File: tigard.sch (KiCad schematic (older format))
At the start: 91 parts, among them J1 USB_C_Receptacle_USB2.0, J2 JTAG, J3 UART, J4 SPI, J5 CORTEX, J6 LA, J7 I2C, Q1 BSH103, SW1 TARGET, SW2 MODE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

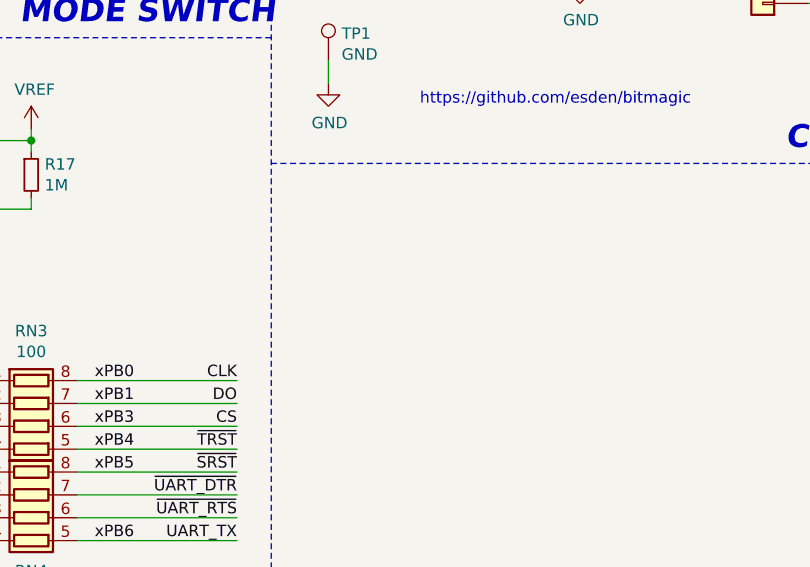
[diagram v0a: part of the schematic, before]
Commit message: Add fidutials
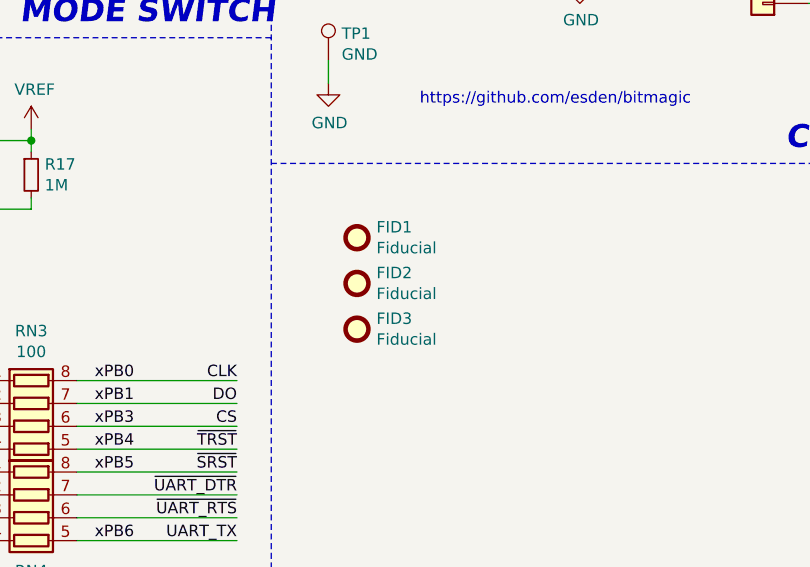
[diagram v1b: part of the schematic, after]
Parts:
- added FID1, FID2, FID3: Fiducial, Fiducial:Fiducial_0.5mm_Mask1mm, symbol Mechanical:Fiducial
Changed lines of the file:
@@
 Wire Wire Line
 	2600 4100 2600 4150
+$Comp
+L Mechanical:Fiducial FID1
+U 1 1 60A39755
+P 9175 4925
+F 0 "FID1" H 9260 4971 50  0000 L CNN
+F 1 "Fiducial" H 9260 4880 50  0000 L CNN
+F 2 "Fiducial:Fiducial_0.5mm_Mask1mm" H 9175 4925 50  0001 C CNN
+F 3 "~" H 9175 4925 50  0001 C CNN
+	1    9175 4925
+	1    0    0    -1
+$EndComp
+$Comp
+L Mechanical:Fiducial FID2
+U 1 1 60A39B2D
+P 9175 5125
+F 0 "FID2" H 9260 5171 50  0000 L CNN
+F 1 "Fiducial" H 9260 5080 50  0000 L CNN
+F 2 "Fiducial:Fiducial_0.5mm_Mask1mm" H 9175 5125 50  0001 C CNN
+F 3 "~" H 9175 5125 50  0001 C CNN
+	1    9175 5125
+	1    0    0    -1
+$EndComp
+$Comp
+L Mechanical:Fiducial FID3
+U 1 1 60A39E45
+P 9175 5325
+F 0 "FID3" H 9260 5371 50  0000 L CNN
+F 1 "Fiducial" H 9260 5280 50  0000 L CNN
+F 2 "Fiducial:Fiducial_0.5mm_Mask1mm" H 9175 5325 50  0001 C CNN
+F 3 "~" H 9175 5325 50  0001 C CNN
+	1    9175 5325
+	1    0    0    -1
+$EndComp
 $EndSCHEMATC
